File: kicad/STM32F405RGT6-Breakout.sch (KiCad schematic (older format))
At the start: 66 parts, among them J1 USB_C_Receptacle_USB2.0, J10 Conn_01x04, J11 Conn_01x03, J2 PWR OUT, J3 SWD/JTAG, J4 USART6, J5 SPI1, J6 I2C1, J7 I2C2, J8 Conn_01x04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

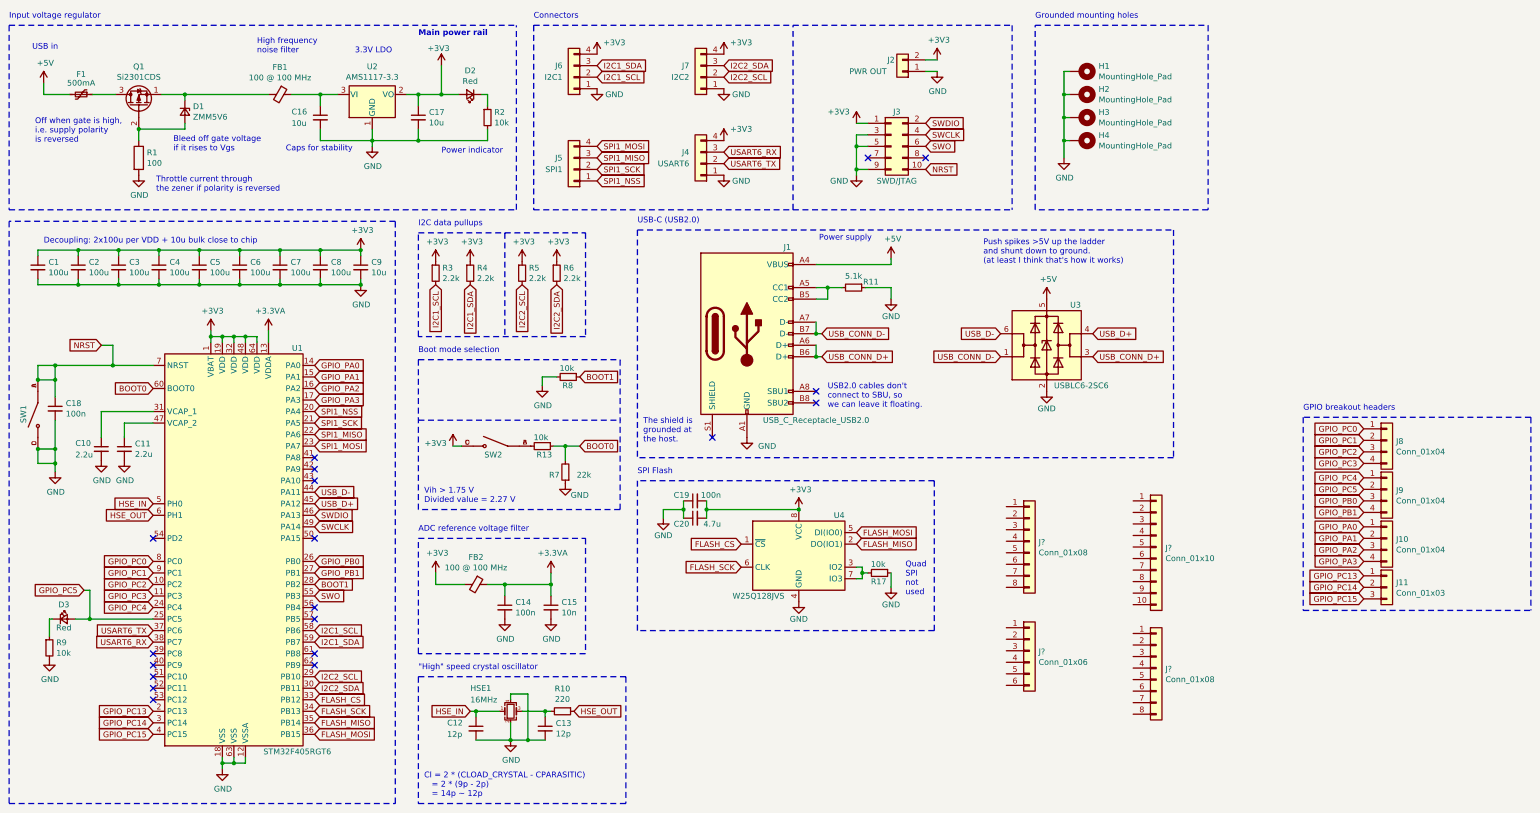
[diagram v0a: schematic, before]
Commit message: Remapped to Uno headers
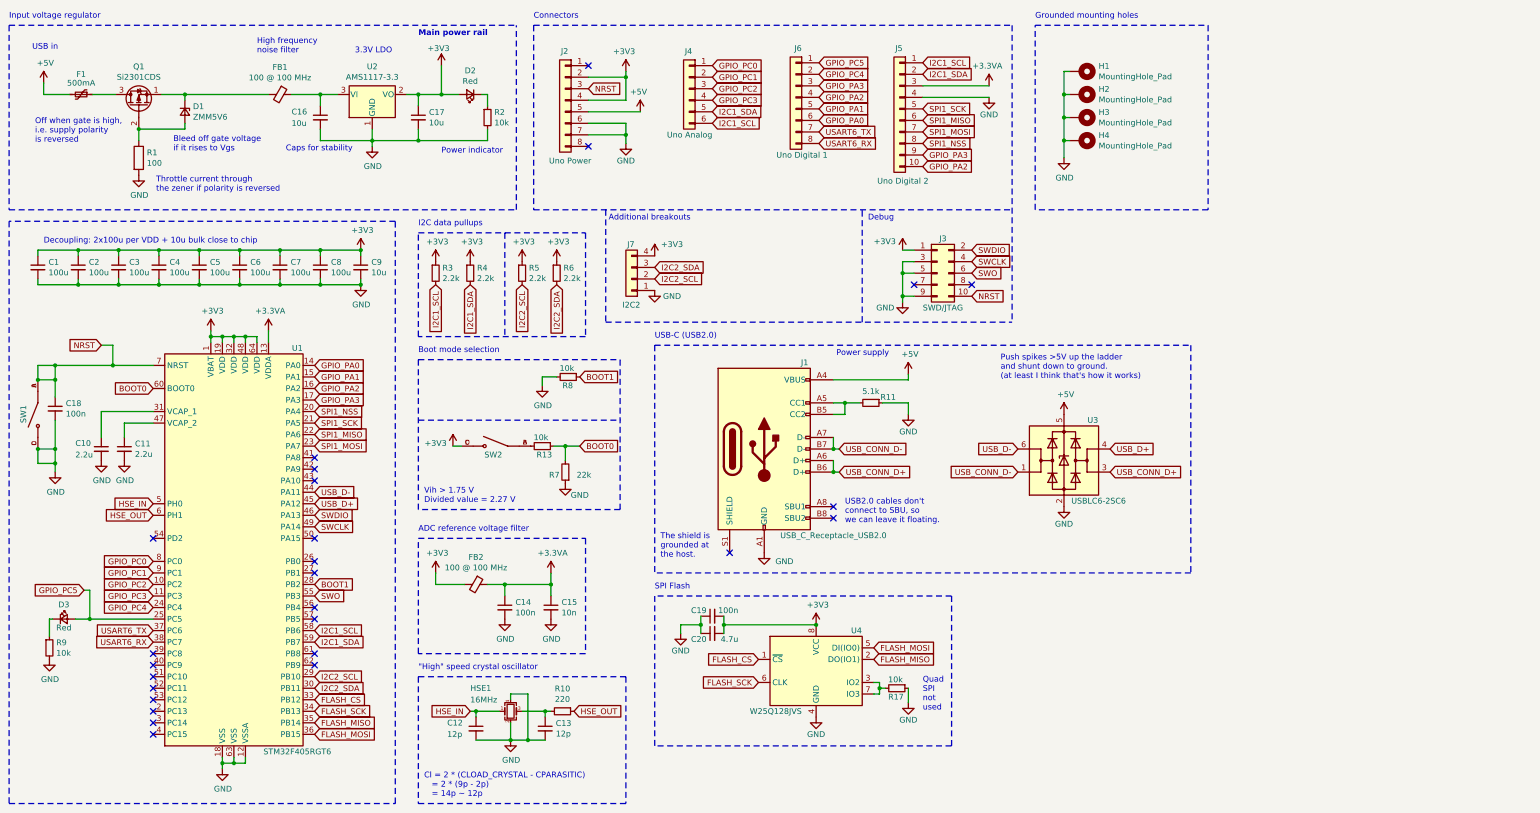
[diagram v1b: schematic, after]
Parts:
- removed J10, J8, J9: Conn_01x04, Connector_PinSocket_2.54mm:PinSocket_1x04_P2.54mm_Vertical_SMD_Pin1Left, symbol Connector_Generic:Conn_01x04
- removed J11: Conn_01x03, Connector_PinSocket_2.54mm:PinSocket_1x03_P2.54mm_Vertical_SMD_Pin1Left, symbol Connector_Generic:Conn_01x03
- removed J2: PWR OUT, Connector_PinSocket_2.54mm:PinSocket_1x02_P2.54mm_Vertical_SMD_Pin1Left, symbol Connector_Generic:Conn_01x02
- removed J4: USART6, Connector_PinSocket_2.54mm:PinSocket_1x04_P2.54mm_Vertical_SMD_Pin1Left, symbol Connector_Generic:Conn_01x04
- removed J5: SPI1, Connector_PinSocket_2.54mm:PinSocket_1x04_P2.54mm_Vertical_SMD_Pin1Left, symbol Connector_Generic:Conn_01x04
- removed J6: I2C1, Connector_PinSocket_2.54mm:PinSocket_1x04_P2.54mm_Vertical_SMD_Pin1Left, symbol Connector_Generic:Conn_01x04
- J2: renamed from J?; value Conn_01x08 -> Uno Power
- J4: renamed from J?; value Conn_01x06 -> Uno Analog
- J5: renamed from J?; value Conn_01x10 -> Uno Digital 2
- J6: renamed from J?; value Conn_01x08 -> Uno Digital 1
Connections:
- net +3.3VA: now also J5.3 (Pin_3)
- net +3V3: now also J2.2 (Pin_2), J2.4 (Pin_4)
- net +5V: now also J2.5 (Pin_5)
- net GND: now also J2.6 (Pin_6), J2.7 (Pin_7), J5.4 (Pin_4)
- net GPIO_PA0: now also J6.6 (Pin_6)
- net GPIO_PA1: now also J6.5 (Pin_5)
- net GPIO_PA2: now also J5.10 (Pin_10), J6.4 (Pin_4)
- net GPIO_PA3: now also J5.9 (Pin_9), J6.3 (Pin_3)
- net GPIO_PC0: now also J4.1 (Pin_1)
- net GPIO_PC1: now also J4.2 (Pin_2)
- net GPIO_PC2: now also J4.3 (Pin_3)
- net GPIO_PC3: now also J4.4 (Pin_4)
- net GPIO_PC4: now also J6.2 (Pin_2)
- net GPIO_PC5: now also J6.1 (Pin_1)
- net I2C1_SCL: now also J4.6 (Pin_6), J5.1 (Pin_1)
- net I2C1_SDA: now also J4.5 (Pin_5), J5.2 (Pin_2)
- net NRST: now also J2.3 (Pin_3)
- net SPI1_MISO: now also J5.6 (Pin_6)
- net SPI1_MOSI: now also J5.7 (Pin_7)
- net SPI1_NSS: now also J5.8 (Pin_8)
- net SPI1_SCK: now also J5.5 (Pin_5)
- net USART6_RX: now also J6.8 (Pin_8)
- net USART6_TX: now also J6.7 (Pin_7)
- net GPIO_PB0: no longer names the net of U1.26 (PB0)
- net GPIO_PB1: no longer names the net of U1.27 (PB1)
- net GPIO_PC13: no longer names the net of U1.2 (PC13)
- net GPIO_PC14: no longer names the net of U1.3 (PC14)
- net GPIO_PC15: no longer names the net of U1.4 (PC15)
- no-connect marks 19 -> 26
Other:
- note added: "Additional breakouts"
- note added: "Debug"
- note removed: "GPIO breakout headers"
- moved on the sheet: C19, C20, J1, J2, J3, J4, J5, J6, J7, R11, R17, U3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

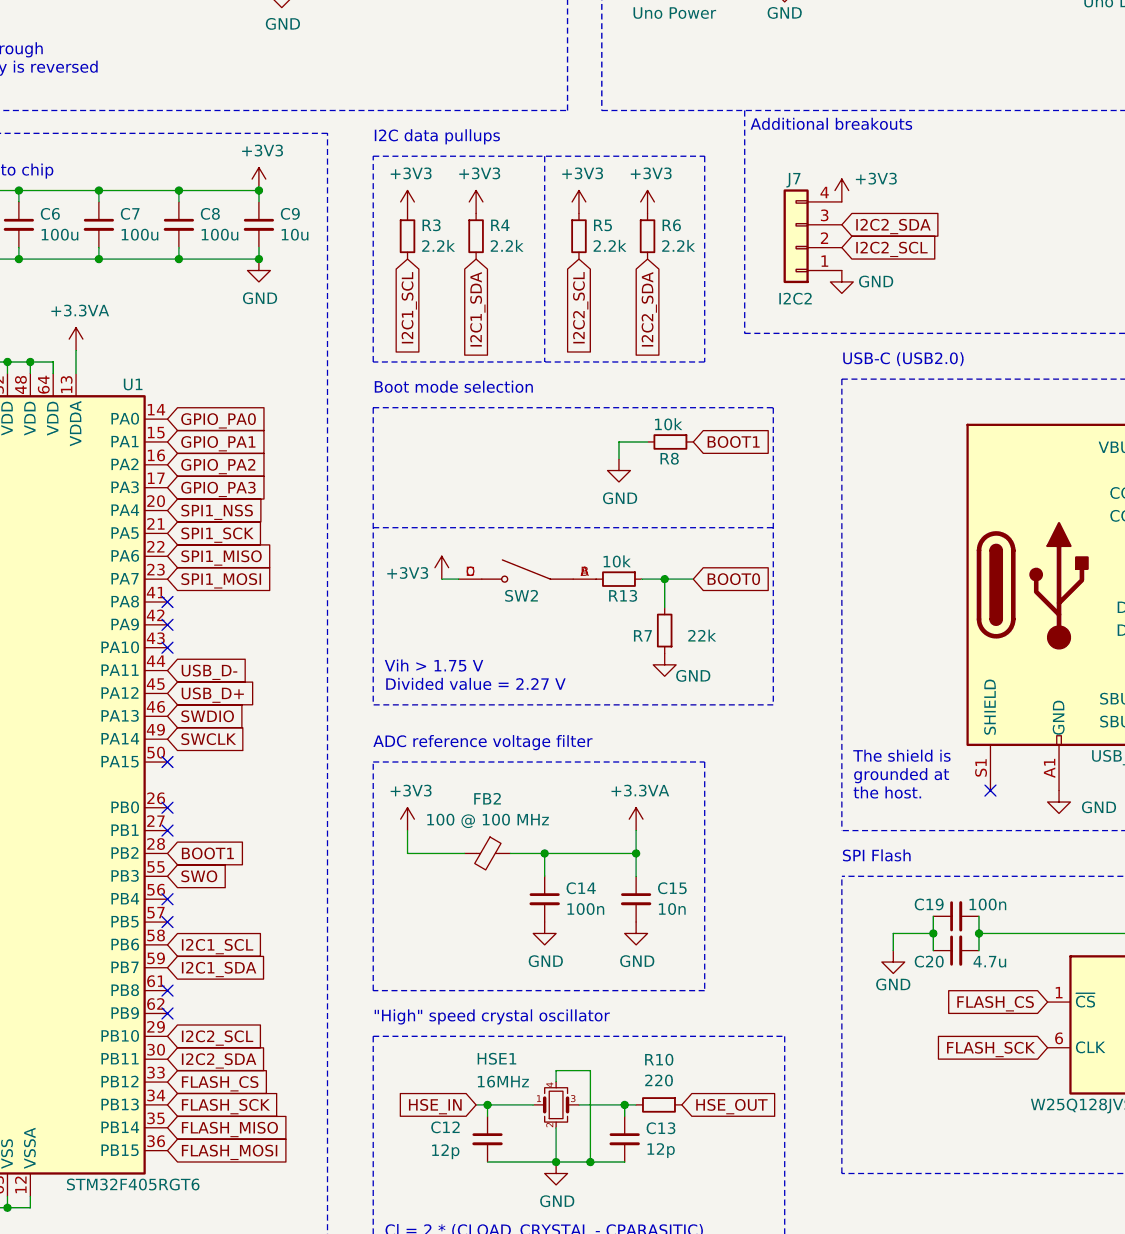
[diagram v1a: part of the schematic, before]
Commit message: - Laid out headers by Uno template - Basic functional component layout - Fixed USB connector clearances to get rid of warnings
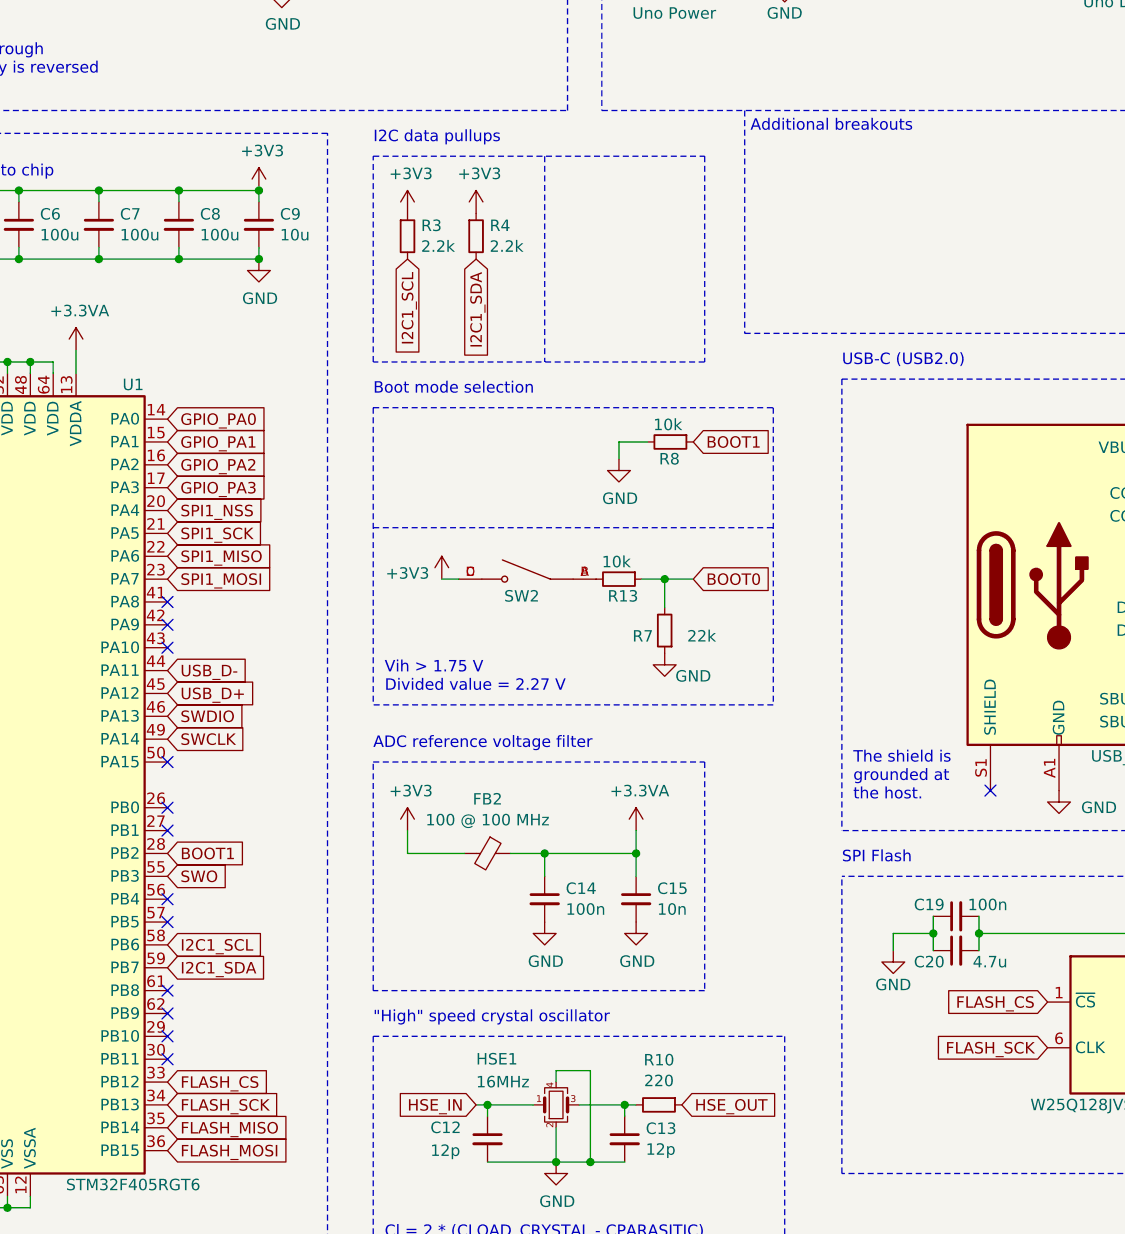
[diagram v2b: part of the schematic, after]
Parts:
- removed J7: I2C2, Connector_PinSocket_2.54mm:PinSocket_1x04_P2.54mm_Vertical_SMD_Pin1Left, symbol Connector_Generic:Conn_01x04
- removed R5, R6: 2.2k, Resistor_SMD:R_0402_1005Metric, symbol Device:R_Small
- H1, H2, H3, H4: footprint MountingHole:MountingHole_4.3mm_M4_Pad_Via -> MountingHole:MountingHole_3.2mm_M3_Pad_Via
- J2, J6: footprint (none) -> Connector_PinSocket_2.54mm:PinSocket_1x08_P2.54mm_Vertical_SMD_Pin1Left
- J4: footprint (none) -> Connector_PinSocket_2.54mm:PinSocket_1x06_P2.54mm_Vertical_SMD_Pin1Left
- J5: footprint (none) -> Connector_PinSocket_2.54mm:PinSocket_1x10_P2.54mm_Vertical_SMD_Pin1Left
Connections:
- net I2C2_SCL: no longer names the net of U1.29 (PB10)
- net I2C2_SDA: no longer names the net of U1.30 (PB11)
- no-connect marks 26 -> 28
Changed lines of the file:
@@
 Text GLabel 3300 6100 2    50   Input ~ 0
 I2C1_SDA
-Text GLabel 3300 6400 2    50   Input ~ 0
-I2C2_SCL
-Text GLabel 3300 6500 2    50   Input ~ 0
-I2C2_SDA
 Text GLabel 1900 6000 0    50   Input ~ 0
 USART6_TX
@@
 F 0 "H3" V 9904 1700 50  0000 L CNN
 F 1 "MountingHole_Pad" V 9995 1700 50  0000 L CNN
-F 2 "MountingHole:MountingHole_4.3mm_M4_Pad_Via" H 9950 1550 50  0001 C CNN
+F 2 "MountingHole:MountingHole_3.2mm_M3_Pad_Via" H 9950 1550 50  0001 C CNN
 F 3 "~" H 9950 1550 50  0001 C CNN
 	1    9950 1550
@@
 F 0 "H4" V 9904 1900 50  0000 L CNN
 F 1 "MountingHole_Pad" V 9995 1900 50  0000 L CNN
-F 2 "MountingHole:MountingHole_4.3mm_M4_Pad_Via" H 9950 1750 50  0001 C CNN
+F 2 "MountingHole:MountingHole_3.2mm_M3_Pad_Via" H 9950 1750 50  0001 C CNN
 F 3 "~" H 9950 1750 50  0001 C CNN
 	1    9950 1750
@@
 F 0 "H2" V 9904 1500 50  0000 L CNN
 F 1 "MountingHole_Pad" V 9995 1500 50  0000 L CNN
-F 2 "MountingHole:MountingHole_4.3mm_M4_Pad_Via" H 9950 1350 50  0001 C CNN
+F 2 "MountingHole:MountingHole_3.2mm_M3_Pad_Via" H 9950 1350 50  0001 C CNN
 F 3 "~" H 9950 1350 50  0001 C CNN
 	1    9950 1350
@@
 F 0 "H1" V 9904 1300 50  0000 L CNN
 F 1 "MountingHole_Pad" V 9995 1300 50  0000 L CNN
-F 2 "MountingHole:MountingHole_4.3mm_M4_Pad_Via" H 9950 1150 50  0001 C CNN
+F 2 "MountingHole:MountingHole_3.2mm_M3_Pad_Via" H 9950 1150 50  0001 C CNN
 F 3 "~" H 9950 1150 50  0001 C CNN
 	1    9950 1150
@@
 Text Notes 6250 3475 0    50   ~ 0
 USB-C (USB2.0)
-$Comp
-L Device:R_Small R6
-U 1 1 61C15D39
-P 5400 2900
-F 0 "R6" H 5459 2946 50  0000 L CNN
-F 1 "2.2k" H 5459 2855 50  0000 L CNN
-F 2 "Resistor_SMD:R_0402_1005Metric" H 5400 2900 50  0001 C CNN
-F 3 "~" H 5400 2900 50  0001 C CNN
-	1    5400 2900
-	1    0    0    -1
-$EndComp
-$Comp
-L Device:R_Small R5
-U 1 1 61C15D43
-P 5100 2900
-F 0 "R5" H 5159 2946 50  0000 L CNN
-F 1 "2.2k" H 5159 2855 50  0000 L CNN
-F 2 "Resistor_SMD:R_0402_1005Metric" H 5100 2900 50  0001 C CNN
-F 3 "~" H 5100 2900 50  0001 C CNN
-	1    5100 2900
-	1    0    0    -1
-$EndComp
-Text GLabel 5100 3000 3    50   Input ~ 0
-I2C2_SCL
-Text GLabel 5400 3000 3    50   Input ~ 0
-I2C2_SDA
-$Comp
-L power:+3V3 #PWR018
-U 1 1 61C21E76
-P 5100 2800
-F 0 "#PWR018" H 5100 2650 50  0001 C CNN
-F 1 "+3V3" H 5115 2973 50  0000 C CNN
-F 2 "" H 5100 2800 50  0001 C CNN
-F 3 "" H 5100 2800 50  0001 C CNN
-	1    5100 2800
-	1    0    0    -1
-$EndComp
-$Comp
-L power:+3V3 #PWR021
-U 1 1 61C2221C
-P 5400 2800
-F 0 "#PWR021" H 5400 2650 50  0001 C CNN
-F 1 "+3V3" H 5415 2973 50  0000 C CNN
-F 2 "" H 5400 2800 50  0001 C CNN
-F 3 "" H 5400 2800 50  0001 C CNN
-	1    5400 2800
-	1    0    0    -1
-$EndComp
 Wire Notes Line
 	5650 2550 5650 3450
@@
 F 0 "J2" H 5450 1825 50  0000 L CNN
 F 1 "Uno Power" H 5250 875 50  0000 L CNN
-F 2 "" H 5475 1400 50  0001 C CNN
+F 2 "Connector_PinSocket_2.54mm:PinSocket_1x08_P2.54mm_Vertical_SMD_Pin1Left" H 5475 1400 50  0001 C CNN
 F 3 "~" H 5475 1400 50  0001 C CNN
 	1    5475 1400
@@
 F 0 "J6" H 7425 1800 50  0000 L CNN
 F 1 "Uno Digital 1" H 7200 875 50  0000 L CNN
-F 2 "" H 7475 1375 50  0001 C CNN
+F 2 "Connector_PinSocket_2.54mm:PinSocket_1x08_P2.54mm_Vertical_SMD_Pin1Left" H 7475 1375 50  0001 C CNN
 F 3 "~" H 7475 1375 50  0001 C CNN
 	1    7475 1375
@@
 F 0 "J4" H 6525 1625 50  0000 L CNN
 F 1 "Uno Analog" H 6350 900 50  0000 L CNN
-F 2 "" H 6550 1300 50  0001 C CNN
+F 2 "Connector_PinSocket_2.54mm:PinSocket_1x06_P2.54mm_Vertical_SMD_Pin1Left" H 6550 1300 50  0001 C CNN
 F 3 "~" H 6550 1300 50  0001 C CNN
 	1    6550 1300
@@
 F 0 "J5" H 8350 2000 50  0000 L CNN
 F 1 "Uno Digital 2" H 8125 850 50  0000 L CNN
-F 2 "" H 8375 1475 50  0001 C CNN
+F 2 "Connector_PinSocket_2.54mm:PinSocket_1x10_P2.54mm_Vertical_SMD_Pin1Left" H 8375 1475 50  0001 C CNN
 F 3 "~" H 8375 1475 50  0001 C CNN
 	1    8375 1475
@@
 Text GLabel 7675 1175 2    50   Input ~ 0
 GPIO_PC4
-$Comp
-L power:GND #PWR032
-U 1 1 61E55AA2
-P 6250 3050
-F 0 "#PWR032" H 6250 2800 50  0001 C CNN
-F 1 "GND" H 6400 3000 50  0000 C CNN
-F 2 "" H 6250 3050 50  0001 C CNN
-F 3 "" H 6250 3050 50  0001 C CNN
-	1    6250 3050
-	1    0    0    -1
-$EndComp
-$Comp
-L power:+3V3 #PWR031
-U 1 1 61E54E72
-P 6250 2750
-F 0 "#PWR031" H 6250 2600 50  0001 C CNN
-F 1 "+3V3" H 6400 2850 50  0000 C CNN
-F 2 "" H 6250 2750 50  0001 C CNN
-F 3 "" H 6250 2750 50  0001 C CNN
-	1    6250 2750
-	1    0    0    -1
-$EndComp
-$Comp
-L Connector_Generic:Conn_01x04 J7
-U 1 1 61DC0149
-P 6050 2950
-F 0 "J7" H 6025 2650 50  0000 L CNN
-F 1 "I2C2" H 5975 3175 50  0000 L CNN
-F 2 "Connector_PinSocket_2.54mm:PinSocket_1x04_P2.54mm_Vertical_SMD_Pin1Left" H 6050 2950 50  0001 C CNN
-F 3 "~" H 6050 2950 50  0001 C CNN
-	1    6050 2950
-	-1   0    0    1
-$EndComp
-Text GLabel 6250 2850 2    50   Input ~ 0
-I2C2_SDA
-Text GLabel 6250 2950 2    50   Input ~ 0
-I2C2_SCL
 NoConn ~ 1900 6700
 NoConn ~ 1900 6800
@@
 	1    0    0    -1
 $EndComp
+NoConn ~ 3300 6400
+NoConn ~ 3300 6500
 $EndSCHEMATC

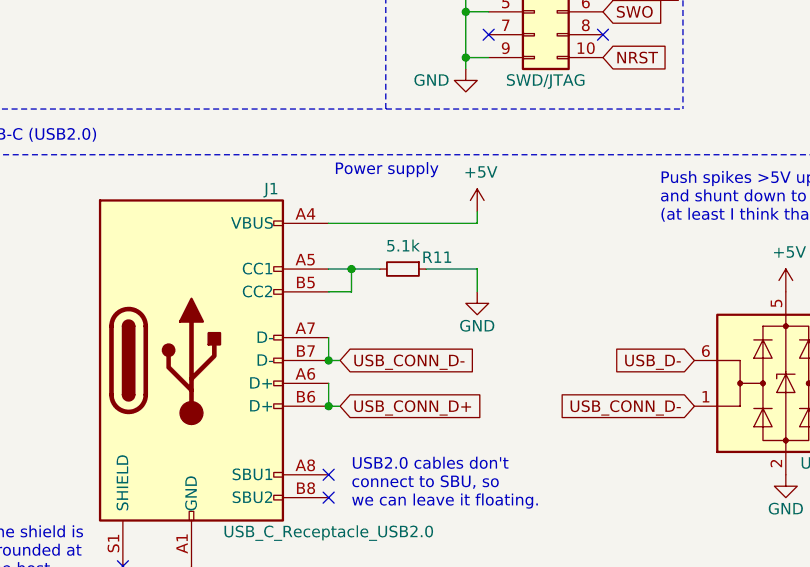
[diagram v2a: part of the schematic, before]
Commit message: Crystal ground
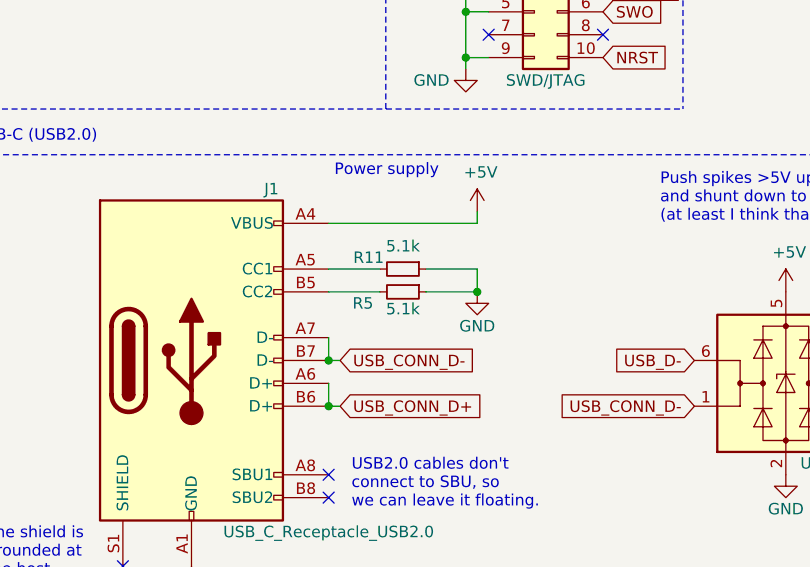
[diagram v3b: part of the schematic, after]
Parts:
- added R5: 5.1k, Resistor_SMD:R_0402_1005Metric, symbol Device:R_Small
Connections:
- net GND: now also R5.1
- net at J1.A5 (CC1), R11.2: no longer J1.B5 (CC2)
- new net: J1.B5 (CC2), R5.2
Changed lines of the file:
@@
 USB_CONN_D+
 Wire Wire Line
-	7800 4025 7900 4025
-Wire Wire Line
-	7800 4125 7900 4125
+	7800 4125 8025 4125
 Wire Wire Line
 	8225 4025 8450 4025
-Wire Wire Line
-	8450 4025 8450 4125
 $Comp
 L power:GND #PWR037
@@
 U 1 1 61FB8501
 P 8125 4025
-F 0 "R11" V 8075 4175 50  0000 C CNN
+F 0 "R11" V 8075 3875 50  0000 C CNN
 F 1 "5.1k" V 8025 4025 50  0000 C CNN
 F 2 "Resistor_SMD:R_0402_1005Metric" H 8125 4025 50  0001 C CNN
@@
 Wire Wire Line
 	8200 6500 8200 6550
-Wire Wire Line
-	7900 4025 7900 4125
-Connection ~ 7900 4025
-Wire Wire Line
-	7900 4025 8025 4025
 Text GLabel 1900 5500 0    50   Input ~ 0
 GPIO_PC1
@@
 NoConn ~ 3300 6400
 NoConn ~ 3300 6500
+$Comp
+L Device:R_Small R5
+U 1 1 61F82455
+P 8125 4125
+F 0 "R5" V 8175 3950 50  0000 C CNN
+F 1 "5.1k" V 8200 4125 50  0000 C CNN
+F 2 "Resistor_SMD:R_0402_1005Metric" H 8125 4125 50  0001 C CNN
+F 3 "~" H 8125 4125 50  0001 C CNN
+	1    8125 4125
+	0    1    1    0
+$EndComp
+Wire Wire Line
+	7800 4025 8025 4025
+Wire Wire Line
+	8450 4025 8450 4125
+Wire Wire Line
+	8225 4125 8450 4125
+Connection ~ 8450 4125
 $EndSCHEMATC
